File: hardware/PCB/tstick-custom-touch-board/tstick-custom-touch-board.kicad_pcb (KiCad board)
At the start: 2 copper layers, 107.3 x 31.8 mm, 21 parts, among them IC1 CY8C206X6A

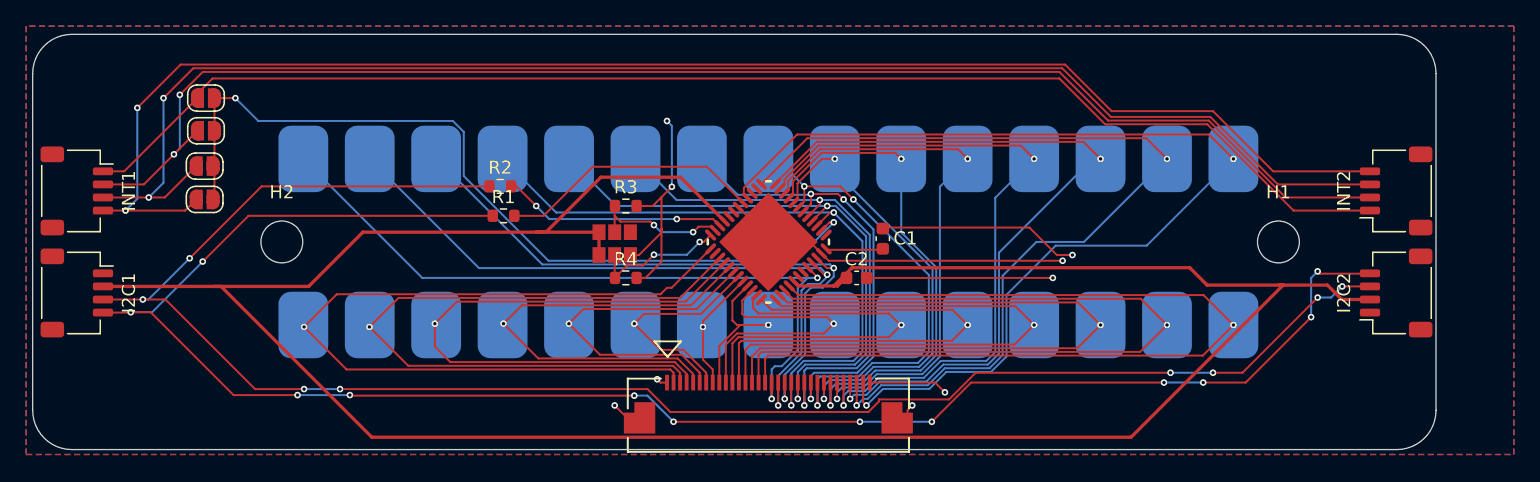
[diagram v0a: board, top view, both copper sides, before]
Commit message: added 3d models, minimised size of paper connector trill board, added pictures
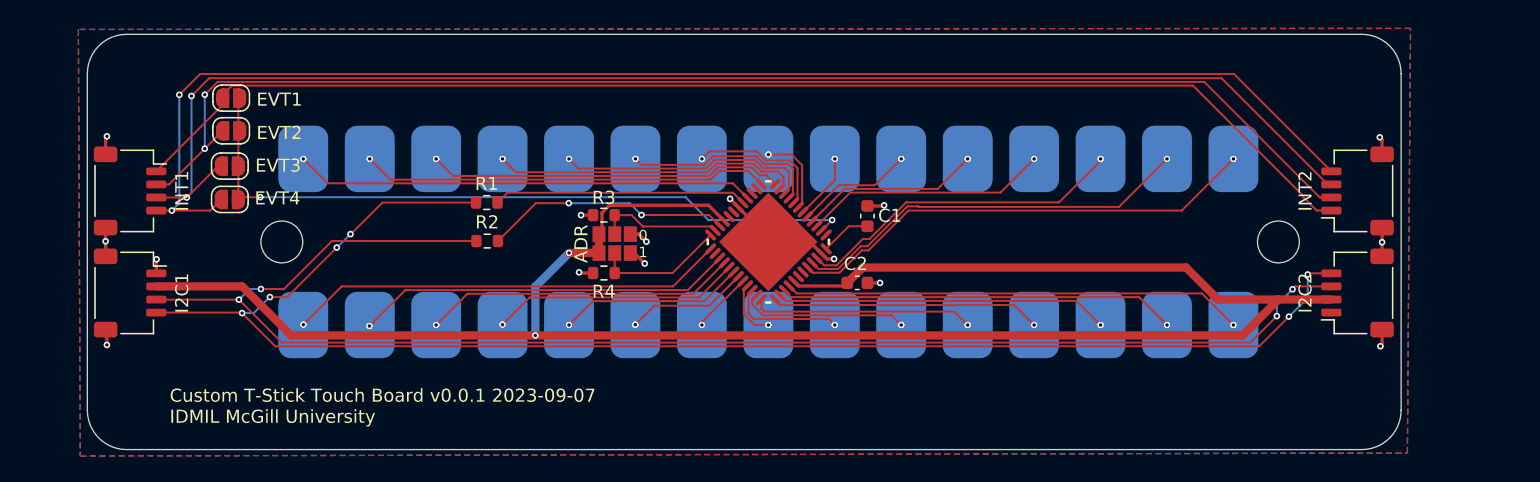
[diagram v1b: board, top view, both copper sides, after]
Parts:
- removed FFC1: Conn_01x32, molex-ffc-connectors:CON_541323262_MOL
- moved R2 4.30 mm to (107.8, 90.7)
- moved I2C1 4.08 mm to (80.5, 94.7)
- moved INT1 4.08 mm to (80.5, 86.8)
- moved I2C2 2.95 mm to (174.3, 94.7)
- moved INT2 2.95 mm to (174.3, 86.8)
- moved C1 2.09 mm to (136.8, 88.8)
- moved JP1 1.92 mm to (88.2, 79.8)
- moved JP2 1.92 mm to (88.2, 82.2)
- moved JP3 1.92 mm to (88.1, 85.0)
- moved JP4 1.92 mm to (88.1, 87.5)
- moved R3 1.82 mm to (116.7, 88.7), turned to 180 degrees
- moved R4 1.72 mm to (116.7, 93.1), turned to 180 degrees
- moved R1 1.63 mm to (107.7, 87.7)
- moved C2 0.38 mm to (136.1, 93.9)
- moved JP1B1 0.15 mm to (116.3, 91.6)
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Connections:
- TOUCH1 pad 16: /TOUCH15 -> /TOUCH29
- TOUCH1 pad 17: /TOUCH16 -> /TOUCH28
- TOUCH1 pad 18: /TOUCH17 -> /TOUCH27
- TOUCH1 pad 19: /TOUCH18 -> /TOUCH26
- TOUCH1 pad 20: /TOUCH19 -> /TOUCH25
- TOUCH1 pad 21: /TOUCH20 -> /TOUCH24
- TOUCH1 pad 22: /TOUCH21 -> /TOUCH23
- TOUCH1 pad 24: /TOUCH23 -> /TOUCH21
- TOUCH1 pad 25: /TOUCH24 -> /TOUCH20
- TOUCH1 pad 26: /TOUCH25 -> /TOUCH19
- TOUCH1 pad 27: /TOUCH26 -> /TOUCH18
- TOUCH1 pad 28: /TOUCH27 -> /TOUCH17
- TOUCH1 pad 29: /TOUCH28 -> /TOUCH16
- TOUCH1 pad 30: /TOUCH29 -> /TOUCH15
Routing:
- net GND: track 88.4 -> 28.1 mm, vias 9 -> 15
- net /TOUCH29: track 81.3 -> 35.2 mm, vias 2 -> 1
- net +3V3: track 197.5 -> 154.3 mm, vias 0 -> 2
- net /TOUCH14: track 73.9 -> 35.2 mm
- net /TOUCH28: track 70.0 -> 31.3 mm, vias 2 -> 1
- net /TOUCH13: track 64.6 -> 30.3 mm
- net /TOUCH20: track 41.1 -> 8.98 mm, vias 2 -> 1
- net /TOUCH27: track 59.3 -> 27.3 mm, vias 2 -> 1
- net /TOUCH18: track 50.6 -> 18.7 mm, vias 2 -> 1
- net /TOUCH19: track 44.9 -> 13.9 mm, vias 2 -> 1
- net /TOUCH0: track 64.2 -> 33.6 mm
- net /TOUCH22: track 36.8 -> 6.25 mm, vias 3 -> 1
- net /TOUCH21: track 35.1 -> 5.06 mm, vias 3 -> 1
- net /TOUCH12: track 55.1 -> 25.5 mm
- net /TOUCH26: track 52.9 -> 23.6 mm, vias 2 -> 1
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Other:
- board size 107.3 x 31.8 mm -> 100.4 x 31.8 mm
- board text added: "0 1"
- board text added: "ADR"
- board text added: "Custom T-Stick Touch Board v0.0.1 2023-09-07 IDMIL McGill University"
- board text added: "EVT1"
- board text added: "EVT2"
- board text added: "EVT3"
- board text added: "EVT4"
